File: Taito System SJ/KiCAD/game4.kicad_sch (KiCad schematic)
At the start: 21 parts, among them U44 74LS74, U46 74LS74, U56 74LS273, U66 74LS32, U66 74LS367, U67 82S09, U68 74LS08

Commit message: Multiple updates while coding core
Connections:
- net D0: now also U46.2 (D)
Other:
- moved on the sheet: U46A
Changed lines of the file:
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@@
+    (stroke (width 0) (type default))
+  )
+  (bus_entry (at 129.54 116.84) (size -2.54 2.54)
     (stroke (width 0) (type default))
   )
@@
     (stroke (width 0) (type default))
   )
-  (wire (pts (xy 97.79 104.14) (xy 97.79 102.87))
+  (wire (pts (xy 113.03 104.14) (xy 113.03 102.87))
     (stroke (width 0) (type default))
   )
@@
     (stroke (width 0) (type default))
   )
+  (wire (pts (xy 96.52 92.71) (xy 96.52 119.38))
+    (stroke (width 0) (type default))
+  )
   (bus (pts (xy 129.54 53.34) (xy 129.54 55.88))
     (stroke (width 0) (type default))
@@
     (stroke (width 0) (type default))
   )
-  (wire (pts (xy 86.36 95.25) (xy 90.17 95.25))
+  (wire (pts (xy 86.36 95.25) (xy 105.41 95.25))
     (stroke (width 0) (type default))
   )
@@
     (stroke (width 0) (type default))
   )
-  (wire (pts (xy 97.79 86.36) (xy 97.79 87.63))
+  (wire (pts (xy 113.03 85.09) (xy 113.03 87.63))
     (stroke (width 0) (type default))
   )
@@
     (stroke (width 0) (type default))
   )
+  (wire (pts (xy 105.41 92.71) (xy 96.52 92.71))
+    (stroke (width 0) (type default))
+  )
   (bus (pts (xy 129.54 45.72) (xy 129.54 48.26))
     (stroke (width 0) (type default))
@@
     (stroke (width 0) (type default))
   )
-  (wire (pts (xy 105.41 92.71) (xy 148.59 92.71))
+  (wire (pts (xy 120.65 92.71) (xy 148.59 92.71))
     (stroke (width 0) (type default))
   )
@@
     (stroke (width 0) (type default))
   )
-  (bus (pts (xy 129.54 115.57) (xy 129.54 121.92))
+  (bus (pts (xy 129.54 115.57) (xy 129.54 116.84))
     (stroke (width 0) (type default))
   )
@@
     (stroke (width 0) (type default))
   )
+  (bus (pts (xy 129.54 116.84) (xy 129.54 121.92))
+    (stroke (width 0) (type default))
+  )
   (wire (pts (xy 214.63 95.25) (xy 228.6 95.25))
     (stroke (width 0) (type default))
@@
     (stroke (width 0) (type default))
   )
+  (wire (pts (xy 96.52 119.38) (xy 127 119.38))
+    (stroke (width 0) (type default))
+  )
   (wire (pts (xy 148.59 72.39) (xy 123.19 72.39))
     (stroke (width 0) (type default))
@@
   )
   (label "A0" (at 69.85 92.71 180) (fields_autoplaced)
+    (effects (font (size 1.27 1.27)) (justify right bottom))
+  )
+  (label "D0" (at 102.87 92.71 180) (fields_autoplaced)
     (effects (font (size 1.27 1.27)) (justify right bottom))
   )
@@
     )
   )
-  (symbol (lib_id "power:VCC") (at 97.79 104.14 0) (mirror x) (unit 1)
-    (in_bom yes) (on_board yes) (dnp no) (fields_autoplaced)
-    (property "Reference" "#PWR?" (at 97.79 100.33 0)
-      (effects (font (size 1.27 1.27)) hide)
-    )
-    (property "Value" "VCC" (at 97.79 107.7158 0)
+  (symbol (lib_id "power:VCC") (at 113.03 104.14 0) (mirror x) (unit 1)
+    (in_bom yes) (on_board yes) (dnp no) (fields_autoplaced)
+    (property "Reference" "#PWR?" (at 113.03 100.33 0)
+      (effects (font (size 1.27 1.27)) hide)
+    )
+    (property "Value" "VCC" (at 113.03 107.7158 0)
       (effects (font (size 1.27 1.27)))
     )
-    (property "Footprint" "" (at 97.79 104.14 0)
-      (effects (font (size 1.27 1.27)) hide)
-    )
-    (property "Datasheet" "" (at 97.79 104.14 0)
+    (property "Footprint" "" (at 113.03 104.14 0)
+      (effects (font (size 1.27 1.27)) hide)
+    )
+    (property "Datasheet" "" (at 113.03 104.14 0)
       (effects (font (size 1.27 1.27)) hide)
     )
@@
     )
   )
-  (symbol (lib_id "power:VCC") (at 97.79 86.36 0) (unit 1)
-    (in_bom yes) (on_board yes) (dnp no) (fields_autoplaced)
-    (property "Reference" "#PWR?" (at 97.79 90.17 0)
-      (effects (font (size 1.27 1.27)) hide)
-    )
-    (property "Value" "VCC" (at 97.79 82.7842 0)
+  (symbol (lib_id "power:VCC") (at 113.03 85.09 0) (unit 1)
+    (in_bom yes) (on_board yes) (dnp no) (fields_autoplaced)
+    (property "Reference" "#PWR?" (at 113.03 88.9 0)
+      (effects (font (size 1.27 1.27)) hide)
+    )
+    (property "Value" "VCC" (at 113.03 81.5142 0)
       (effects (font (size 1.27 1.27)))
     )
-    (property "Footprint" "" (at 97.79 86.36 0)
-      (effects (font (size 1.27 1.27)) hide)
-    )
-    (property "Datasheet" "" (at 97.79 86.36 0)
+    (property "Footprint" "" (at 113.03 85.09 0)
+      (effects (font (size 1.27 1.27)) hide)
+    )
+    (property "Datasheet" "" (at 113.03 85.09 0)
       (effects (font (size 1.27 1.27)) hide)
     )
@@
     )
   )
-  (symbol (lib_id "jt74:74LS74") (at 97.79 95.25 0) (unit 1)
-    (in_bom yes) (on_board yes) (dnp no) (fields_autoplaced)
-    (property "Reference" "U46" (at 99.8094 86.4702 0)
+  (symbol (lib_id "jt74:74LS74") (at 113.03 95.25 0) (unit 1)
+    (in_bom yes) (on_board yes) (dnp no) (fields_autoplaced)
+    (property "Reference" "U46" (at 115.0494 86.4702 0)
       (effects (font (size 1.27 1.27)) (justify left))
     )
-    (property "Value" "74LS74" (at 99.8094 89.0071 0)
+    (property "Value" "74LS74" (at 115.0494 89.0071 0)
       (effects (font (size 1.27 1.27)) (justify left))
     )
-    (property "Footprint" "" (at 97.79 95.25 0)
-      (effects (font (size 1.27 1.27)) hide)
-    )
-    (property "Datasheet" "74xx/74hc_hct74.pdf" (at 97.79 95.25 0)
-      (effects (font (size 1.27 1.27)) hide)
-    )
+    (property "Footprint" "" (at 113.03 95.25 0)
+      (effects (font (size 1.27 1.27)) hide)
+    )
+    (property "Datasheet" "74xx/74hc_hct74.pdf" (at 113.03 95.25 0)
+      (effects (font (size 1.27 1.27)) hide)
+    )

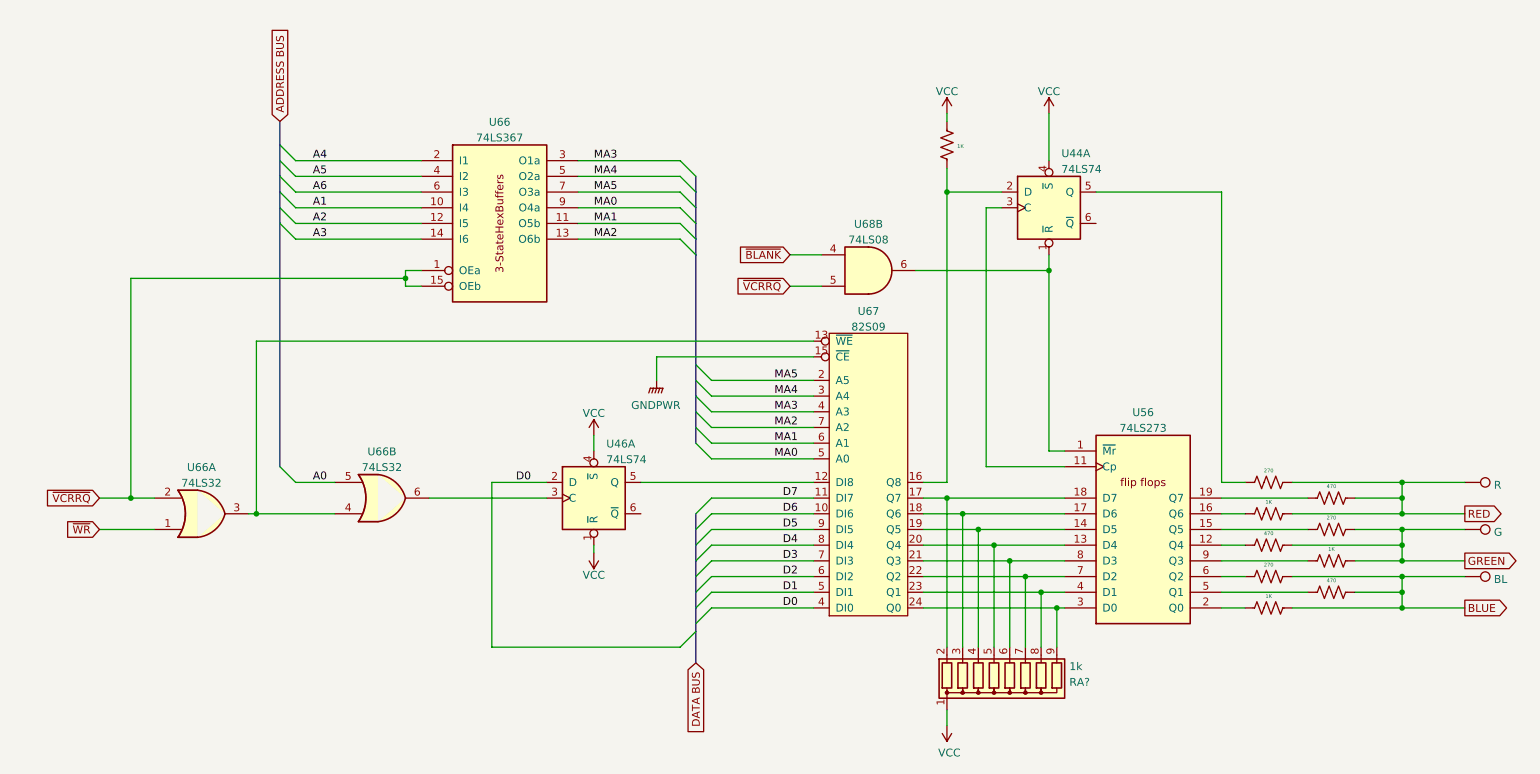
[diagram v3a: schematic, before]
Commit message: Added MCU to Taito SJ Schematics
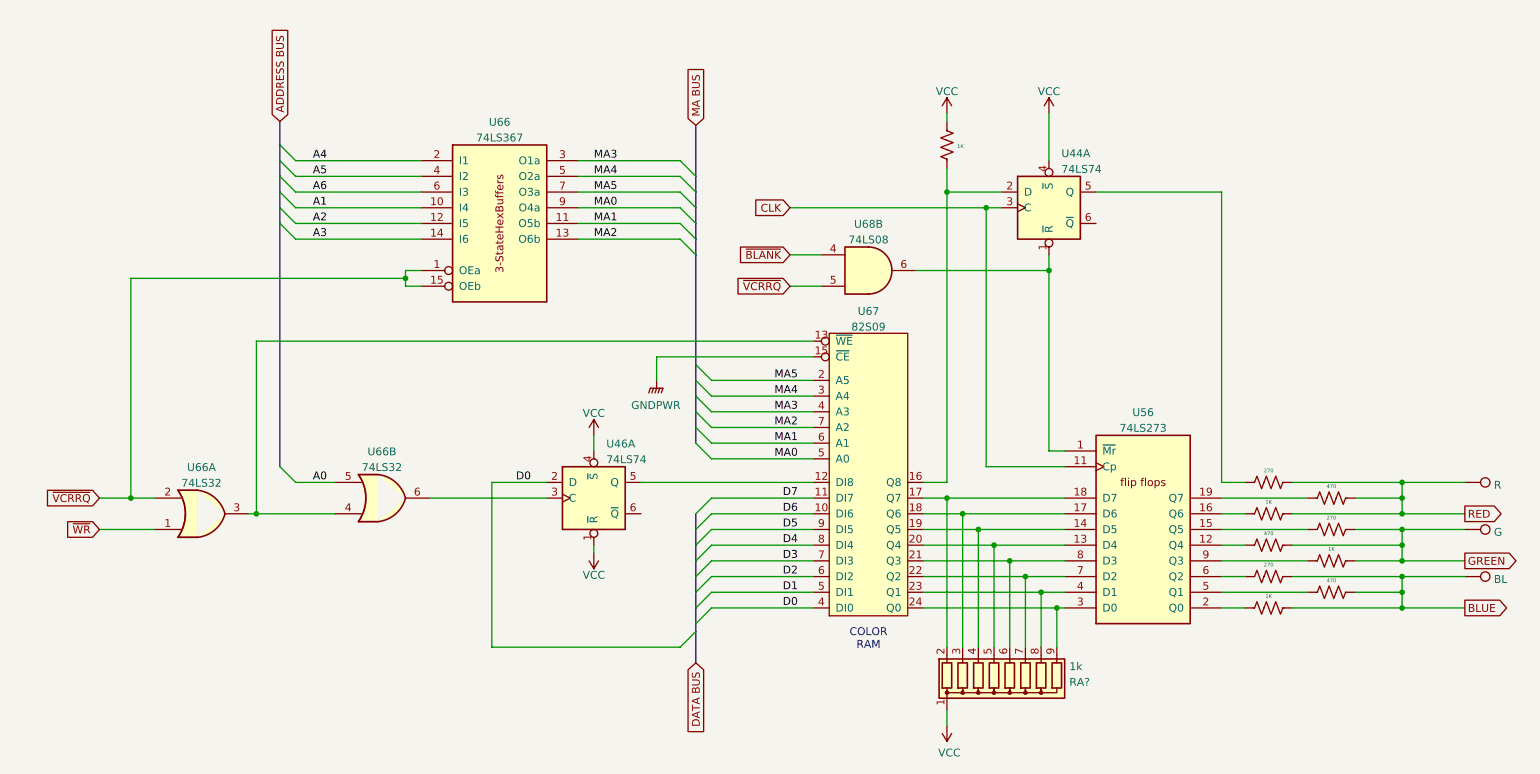
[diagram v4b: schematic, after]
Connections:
- net CLK: now reaches U44.3 (C), U56.11 (Cp)
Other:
- note added: "COLOR RAM"
